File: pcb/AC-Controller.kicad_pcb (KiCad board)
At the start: 2 copper layers, 66 x 67 mm, 79 parts, among them J1 Serial, J2 USB_C_Top, J3 USB_C_Bottom, Q1 AO3400A, Q2 AO3401A, Q5 AO3400A, SW1 Mode, SW2 Value, SW3 RESET, U1 ESP32-WROOM-32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

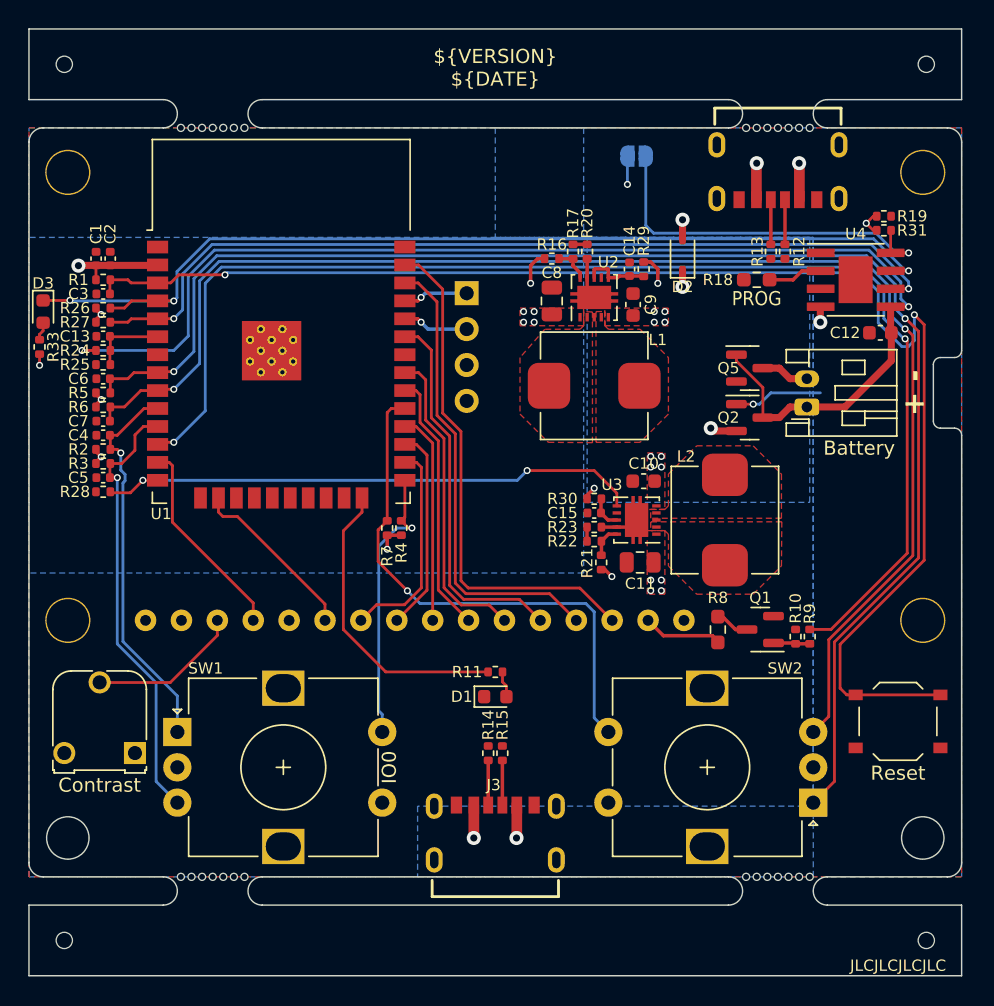
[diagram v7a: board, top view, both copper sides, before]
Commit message: feat: add more ways to wake up
Adding simple MOSFET logic to watch 4 signals for waking up from deep sleep
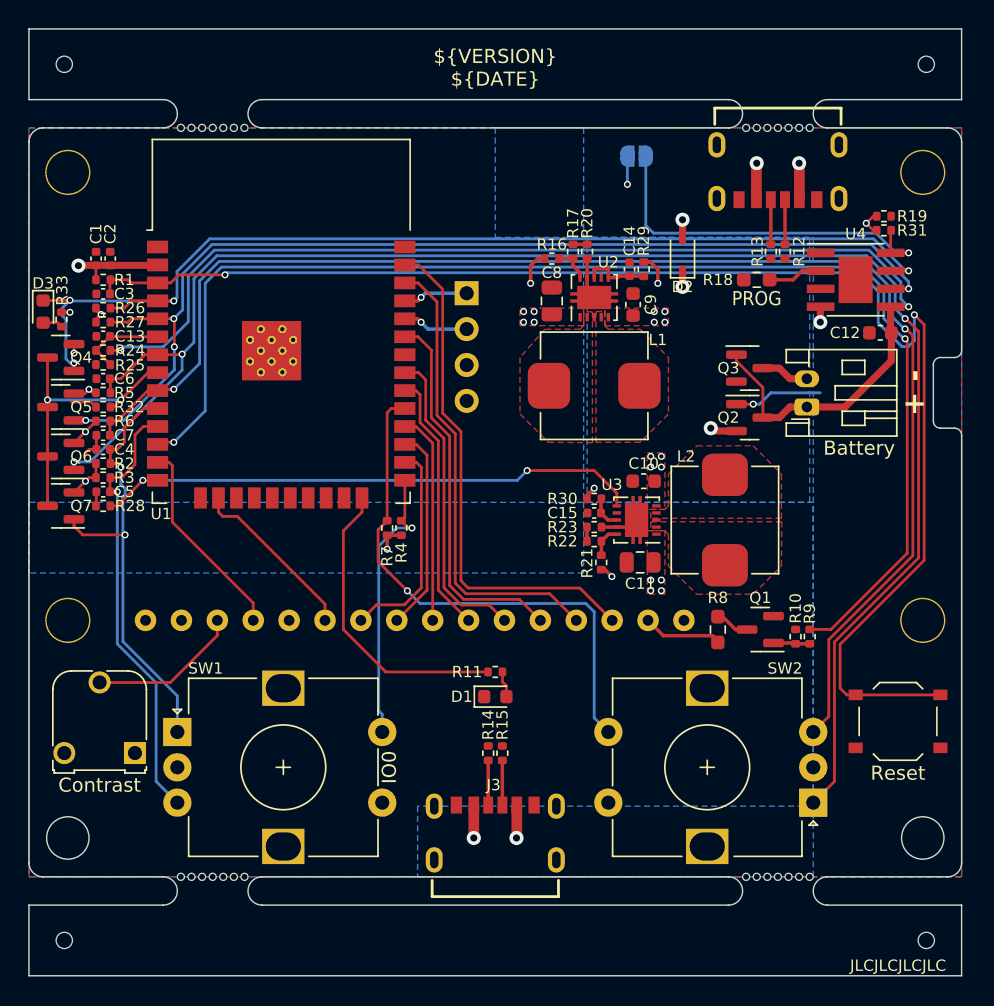
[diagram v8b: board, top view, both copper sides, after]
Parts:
- added Q4: BSS84, Package_TO_SOT_SMD:SOT-23, F.Cu at (119.2, 87.2)
- added Q5: BSS84, Package_TO_SOT_SMD:SOT-23, F.Cu at (119.2, 90.8)
- added Q6: BSS84, Package_TO_SOT_SMD:SOT-23, F.Cu at (119.2, 94.2)
- added Q7: BSS84, Package_TO_SOT_SMD:SOT-23, F.Cu at (119.2, 97.8)
- added R32: 100k, Resistor_SMD:R_0402_1005Metric, F.Cu at (122.2, 90.8)
- moved R33 2.49 mm to (119.3, 84.5), turned to -90 degrees
- moved C4 1.00 mm to (122.2, 93.8)
- moved C5 1.00 mm to (122.2, 96.8)
- moved C7 1.00 mm to (122.2, 92.8)
- moved R2 1.00 mm to (122.2, 94.8)
- moved R28 1.00 mm to (122.2, 97.8)
- moved R3 1.00 mm to (122.2, 95.8)
- moved R6 1.00 mm to (122.2, 91.8)
- turned R24 to 180 degrees
- renumbered Q5 to Q3
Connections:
- net /LCD_LED_K renamed /LCD_K
- U1 pad 7: unconnected-(U1-IO35-Pad7) -> /Encoder2_A
- U1 pad 8: /Encoder2_A -> /WakeUp
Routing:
- net /WakeUp: track 0.00 -> 20.0 mm, vias 0 -> 2
- net /~{Battery_Standby}: track 63.1 -> 75.3 mm, vias 2 -> 4
- net /Encoder2_A: track 104.5 -> 116.2 mm, vias 2 -> 3
- net /~{Battery_Charging}: track 71.1 -> 76.8 mm, vias 3 -> 4
- net GND: track 8.35 -> 13.2 mm
- net +3V3: track 15.8 -> 20.6 mm, vias 11 -> 13
- net /Encoder1_A: track 27.6 -> 32.3 mm, vias 1 -> 2
- net /Battery+: track 88.4 -> 84.8 mm
- net /BattMeasure: track 5.37 -> 6.20 mm
